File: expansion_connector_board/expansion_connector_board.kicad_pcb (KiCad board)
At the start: 2 copper layers, 139 x 87 mm, 6 parts, among them J1 Conn_01x04, J12 Conn_02x17_Top_Bottom, J13 Conn_01x04, J3 Conn_02x17_Top_Bottom

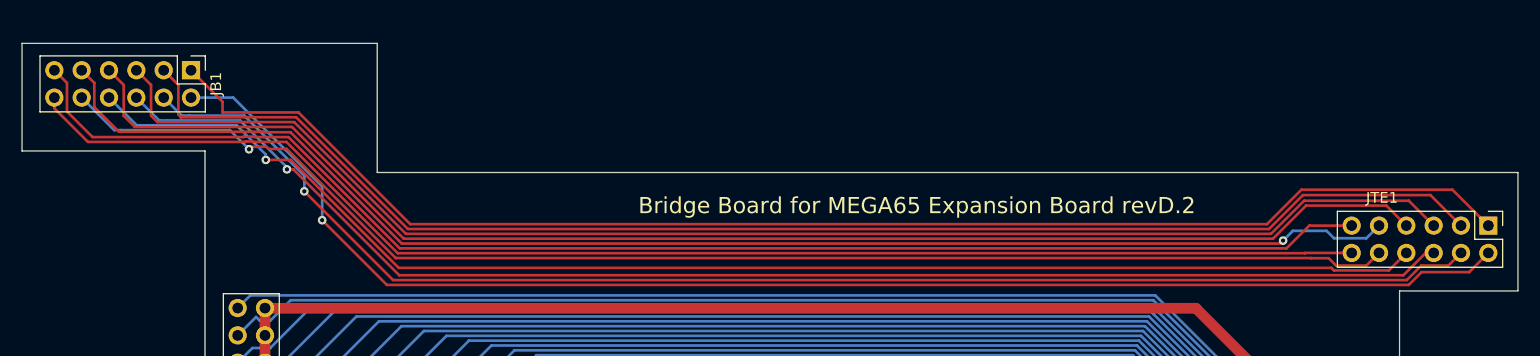
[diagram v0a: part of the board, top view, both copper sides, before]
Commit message: flip J8 and relocate
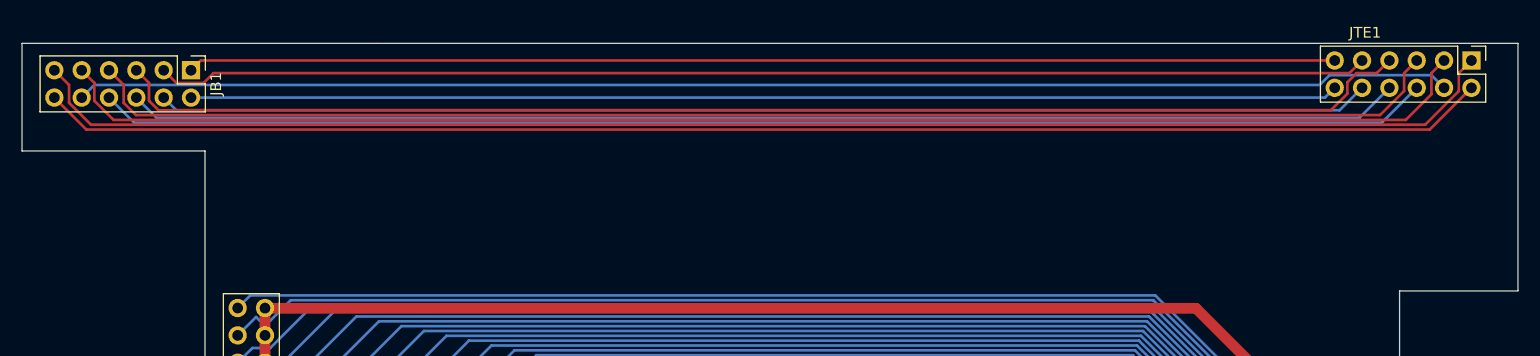
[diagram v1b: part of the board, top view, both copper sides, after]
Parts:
- moved JTE1 15.4 mm to (191.7, 38.6)
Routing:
- net Net-(JB1-Pad2): track 130.8 -> 106.7 mm, vias 1 -> 0
- net Net-(JB1-Pad1): track 129.8 -> 106.7 mm
- net Net-(JB1-Pad3): track 130.8 -> 112.7 mm
- net Net-(JB1-Pad4): track 129.5 -> 112.7 mm, vias 1 -> 0
- net Net-(JB1-Pad6): track 128.4 -> 118.4 mm, vias 1 -> 0
- net Net-(JB1-Pad5): track 130.7 -> 121.5 mm
- net Net-(JB1-Pad11): track 129.9 -> 138.2 mm
- net Net-(JB1-Pad12): track 127.2 -> 134.5 mm
- net Net-(JB1-Pad8): track 128.2 -> 123.8 mm, vias 1 -> 0
- net Net-(JB1-Pad7): track 130.8 -> 127.3 mm
- net Net-(JB1-Pad9): track 129.8 -> 132.9 mm, vias 1 -> 0
- net Net-(JB1-Pad10): track 127.7 -> 127.9 mm, vias 1 -> 0
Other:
- outline, holes or cut-outs redrawn
- board text removed: "Bridge Board for MEGA65 Expansion Board revD.2"

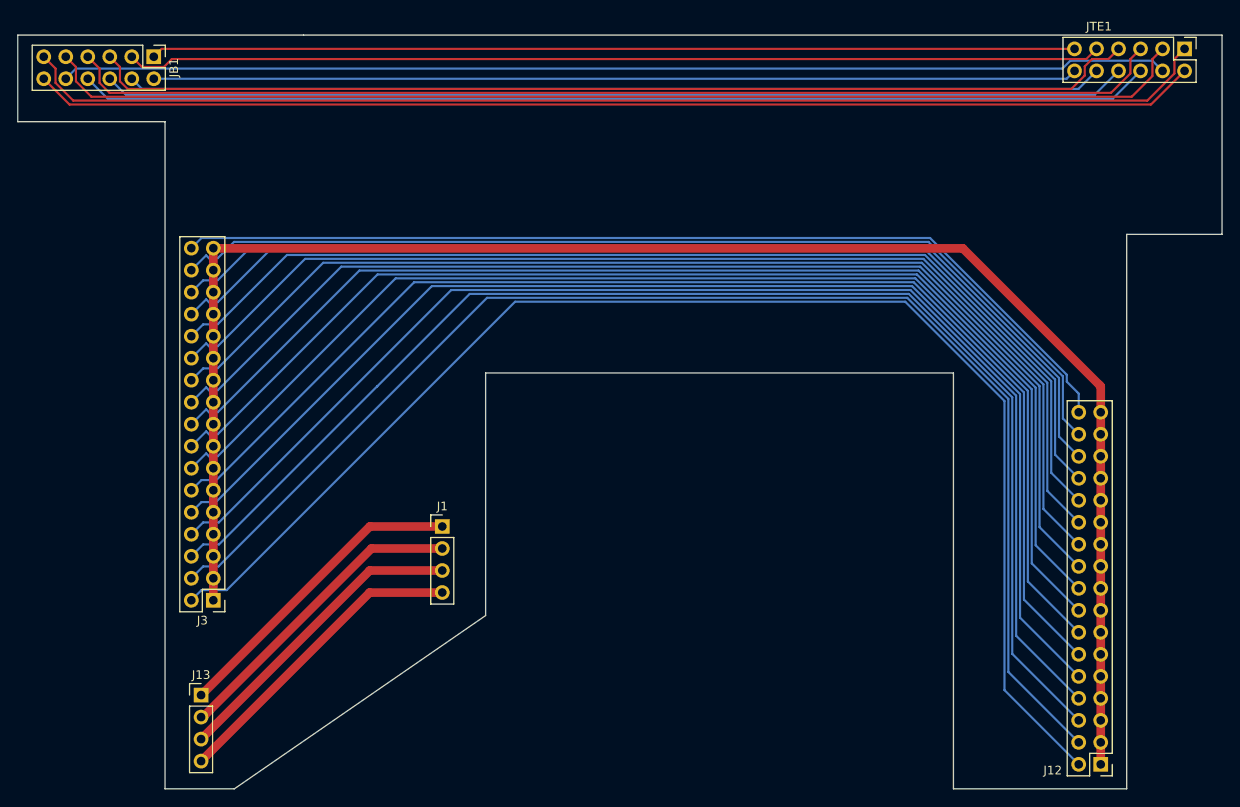
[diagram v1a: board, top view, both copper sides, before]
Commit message: fix rel position of MEGA65 board side connectors
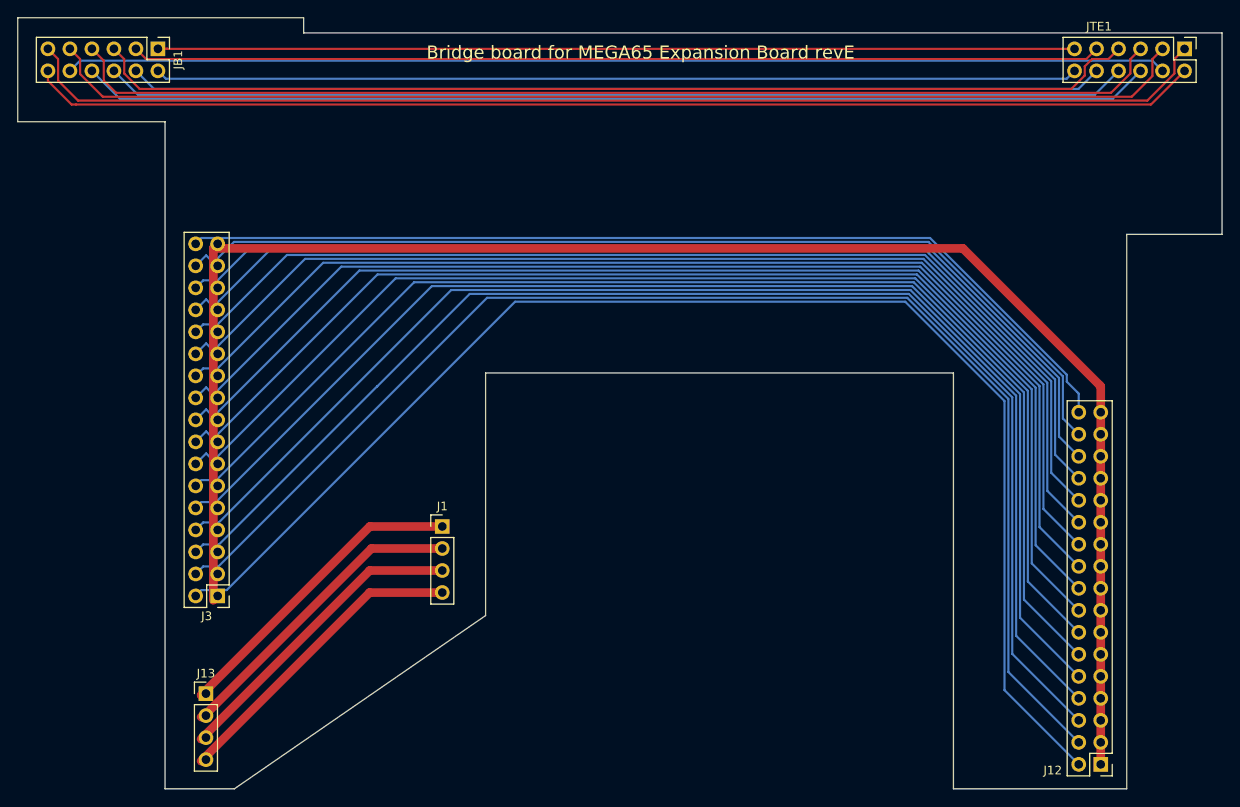
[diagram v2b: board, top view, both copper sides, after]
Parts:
- moved JB1 1.03 mm to (73.2, 38.6)
- moved J3 0.71 mm to (80.1, 101.7)
- moved J13 0.59 mm to (78.7, 113.0)
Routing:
- net Net-(JB1-Pad3): track 112.7 -> 111.9 mm
- net Net-(JB1-Pad10): track 127.9 -> 127.1 mm
- net Net-(JB1-Pad12): track 134.5 -> 135.1 mm
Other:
- board size 139 x 87 mm -> 139 x 89 mm
- board text added: "Bridge board for MEGA65 Expansion Board revE"

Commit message: fill-out size of bridge board to fit wifi etc
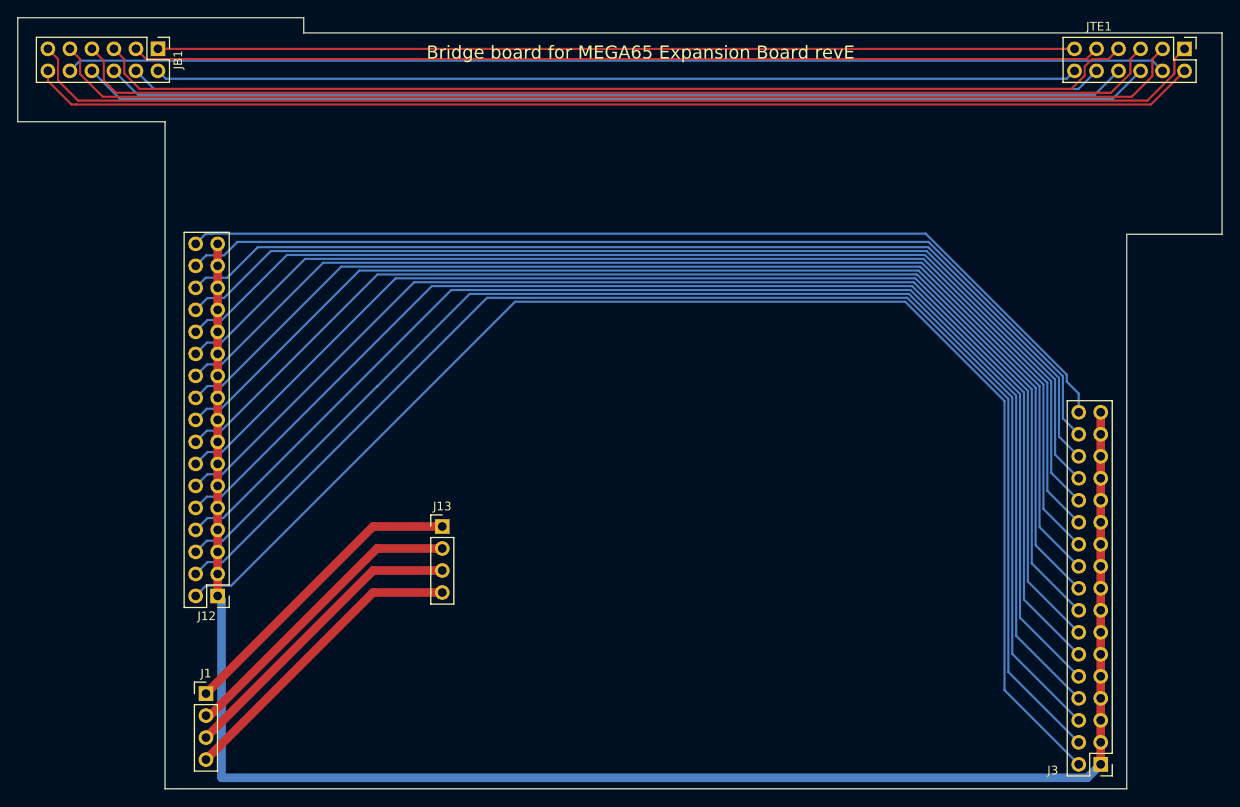
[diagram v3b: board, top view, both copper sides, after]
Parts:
- renumbered J13 to J1, J3 to J12, J1 to J13, J12 to J3
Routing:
- net Net-(J3-Pad1): track 193.3 -> 204.6 mm
- net Net-(J3-Pad28): track 121.7 -> 120.7 mm
- net Net-(J3-Pad18): track 135.9 -> 134.9 mm
- net Net-(J3-Pad24): track 127.4 -> 126.4 mm
- net Net-(J3-Pad20): track 133.1 -> 132.1 mm
- net Net-(J3-Pad16): track 138.8 -> 137.8 mm
- net Net-(J3-Pad14): track 141.6 -> 140.6 mm
- net Net-(J1-Pad2): track 35.9 -> 35.1 mm
- net Net-(J3-Pad8): track 149.9 -> 149.2 mm
- net Net-(J3-Pad4): track 155.6 -> 154.8 mm
- net Net-(J3-Pad22): track 129.9 -> 129.2 mm
- net Net-(J3-Pad2): track 158.4 -> 157.7 mm
- net Net-(J3-Pad26): track 124.2 -> 123.5 mm
- net Net-(J3-Pad12): track 144.2 -> 143.5 mm
- net Net-(J3-Pad6): track 152.7 -> 152.0 mm
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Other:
- outline, holes or cut-outs redrawn

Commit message: work on various checking various measurements
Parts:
- moved JB1 0.07 mm to (73.2, 38.7)
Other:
- board text added: "H4 is here"
- board text added: "Left PMOD on MEGA65 Board"
- board text added: "Left PMOD on expansion board"
